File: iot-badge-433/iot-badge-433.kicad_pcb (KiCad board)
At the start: 2 copper layers, 70 x 100 mm, 68 parts, among them J1 USB_C_Receptacle_USB2.0, J2 Wire ANT, J3 Conn_01x04_Male, Q1 BC847, Q2 BC847, Q3 BC847, SW1 SW_Push, SW2 SW_Push, SW3 SW_Push, SW4 SW_Push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

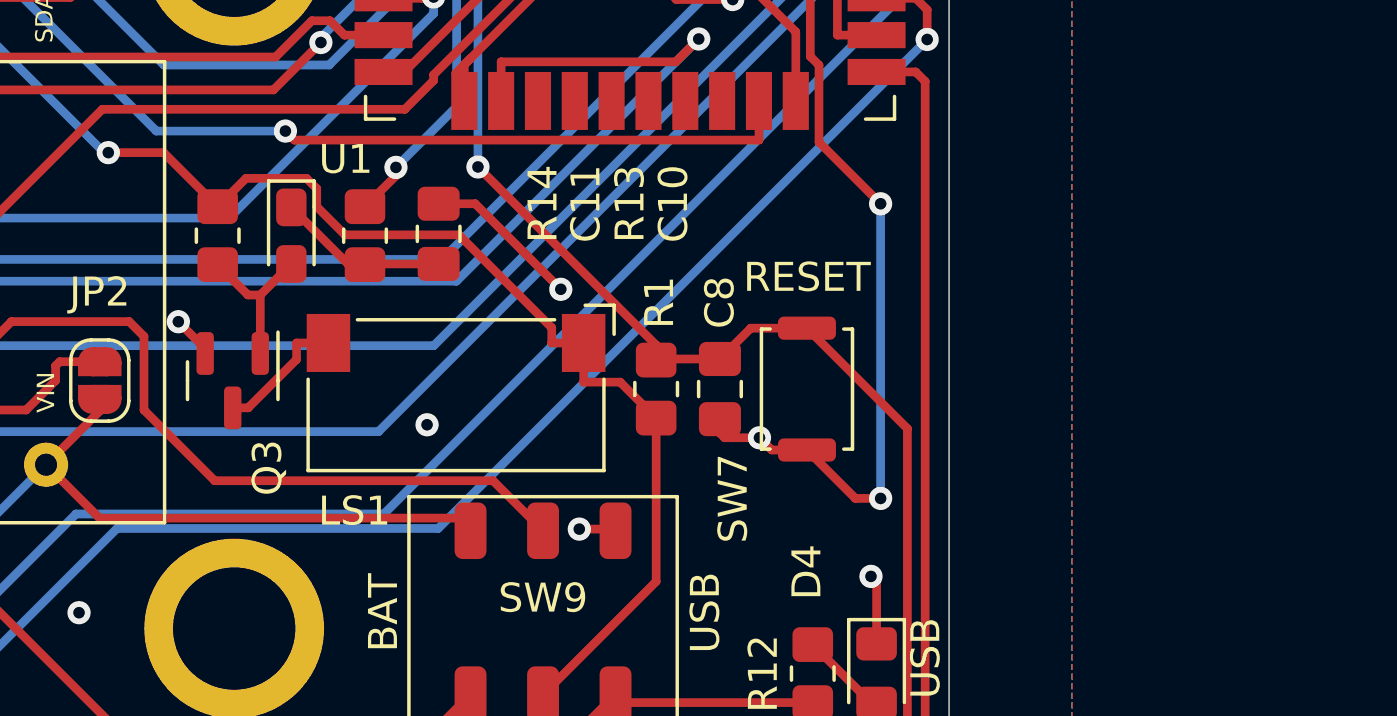
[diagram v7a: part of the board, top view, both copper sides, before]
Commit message: added BTL amp to schematic
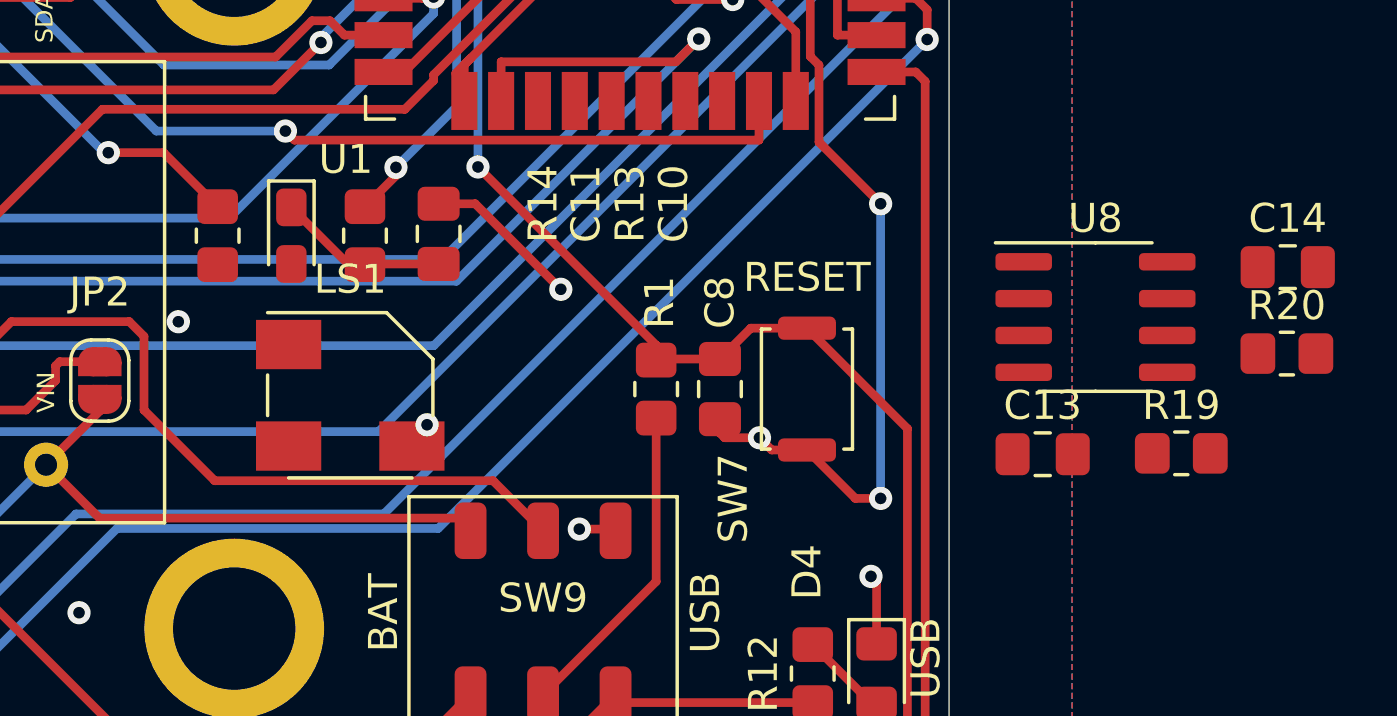
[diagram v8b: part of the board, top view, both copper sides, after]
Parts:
- removed Q3: BC847, Package_TO_SOT_SMD:SOT-23
- added C13: 0.1uF, Capacitor_SMD:C_0805_2012Metric_Pad1.18x1.45mm_HandSolder, F.Cu at (173.2, 97.5)
- added C14: 0.1uF, Capacitor_SMD:C_0805_2012Metric_Pad1.18x1.45mm_HandSolder, F.Cu at (181.7, 91.1)
- added R19: 320, Resistor_SMD:R_0805_2012Metric_Pad1.20x1.40mm_HandSolder, F.Cu at (178.0, 97.5)
- added R20: 20k, Resistor_SMD:R_0805_2012Metric_Pad1.20x1.40mm_HandSolder, F.Cu at (181.6, 94.1)
- added U8: SSM2211S, Package_SO:SOIC-8_3.9x4.9mm_P1.27mm, F.Cu at (175.0, 92.8)
- LS1: value Speaker -> Speaker_SMD; footprint Speaker_SMD:Speaker_SMD-10mmx5mm -> Speaker_SMD:Speaker_SMD-5020
- R13: value 220 -> 620
- R14: value 2.2k -> 20k
- moved LS1 3.65 mm to (149.4, 95.5), turned to 0 degrees
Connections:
- LS1 pad 1: +3V3 -> unconnected-(LS1-Pad1)
- R14 pad 1: +3V3 -> Net-(LS1-Pad2)
- R14 pad 2: Net-(C11-Pad2) -> Net-(R14-Pad2)
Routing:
- net +3V3: track 123.7 -> 103.3 mm
- net Net-(C11-Pad2): track 5.43 -> 0.00 mm
- net Net-(LS1-Pad2): track 4.56 -> 0.00 mm
- net Earth: track 200.3 -> 198.8 mm, vias 97 -> 96
- net Net-(LS1-Pad3): vias 0 -> 1
